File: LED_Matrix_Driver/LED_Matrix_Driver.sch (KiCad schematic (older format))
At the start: 64 parts, among them J1 5V_DC, J2 I2C Bus, J3 LED Anode Rows, J4 Columns 24-31 LED Cathodes, J5 Columns 16-23 LED Cathodes, J6 Columns 8-15 LED Cathodes, J7 Columns 0-7 LED Cathodes, U1 ATmega8-16PU, U2 74HC238, U3 MIC2981, U4 HEF4794B, U5 HEF4794B, U6 HEF4794B, U7 HEF4794B, Y1 16MHz

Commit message: First test commit of ESP32 branch
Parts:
- removed U1: ATmega8-16PU, Package_DIP:DIP-28_W7.62mm_Socket, symbol MCU_Microchip_ATmega:ATmega8-16PU
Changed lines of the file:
@@
 	0    1    1    0
-$EndComp
-$Comp
-L MCU_Microchip_ATmega:ATmega8-16PU U1
-U 1 1 650E955F
-P 3050 5000
-F 0 "U1" H 3050 5000 50  0000 C CNN
-F 1 "ATmega8-16PU" H 3000 4850 50  0000 C CNN
-F 2 "Package_DIP:DIP-28_W7.62mm_Socket" H 3050 5000 50  0001 C CIN
-F 3 "http://ww1.microchip.com/downloads/en/DeviceDoc/atmel-2486-8-bit-avr-microcontroller-atmega8_l_datasheet.pdf" H 3050 5000 50  0001 C CNN
-	1    3050 5000
-	1    0    0    -1
 $EndComp
 Wire Wire Line

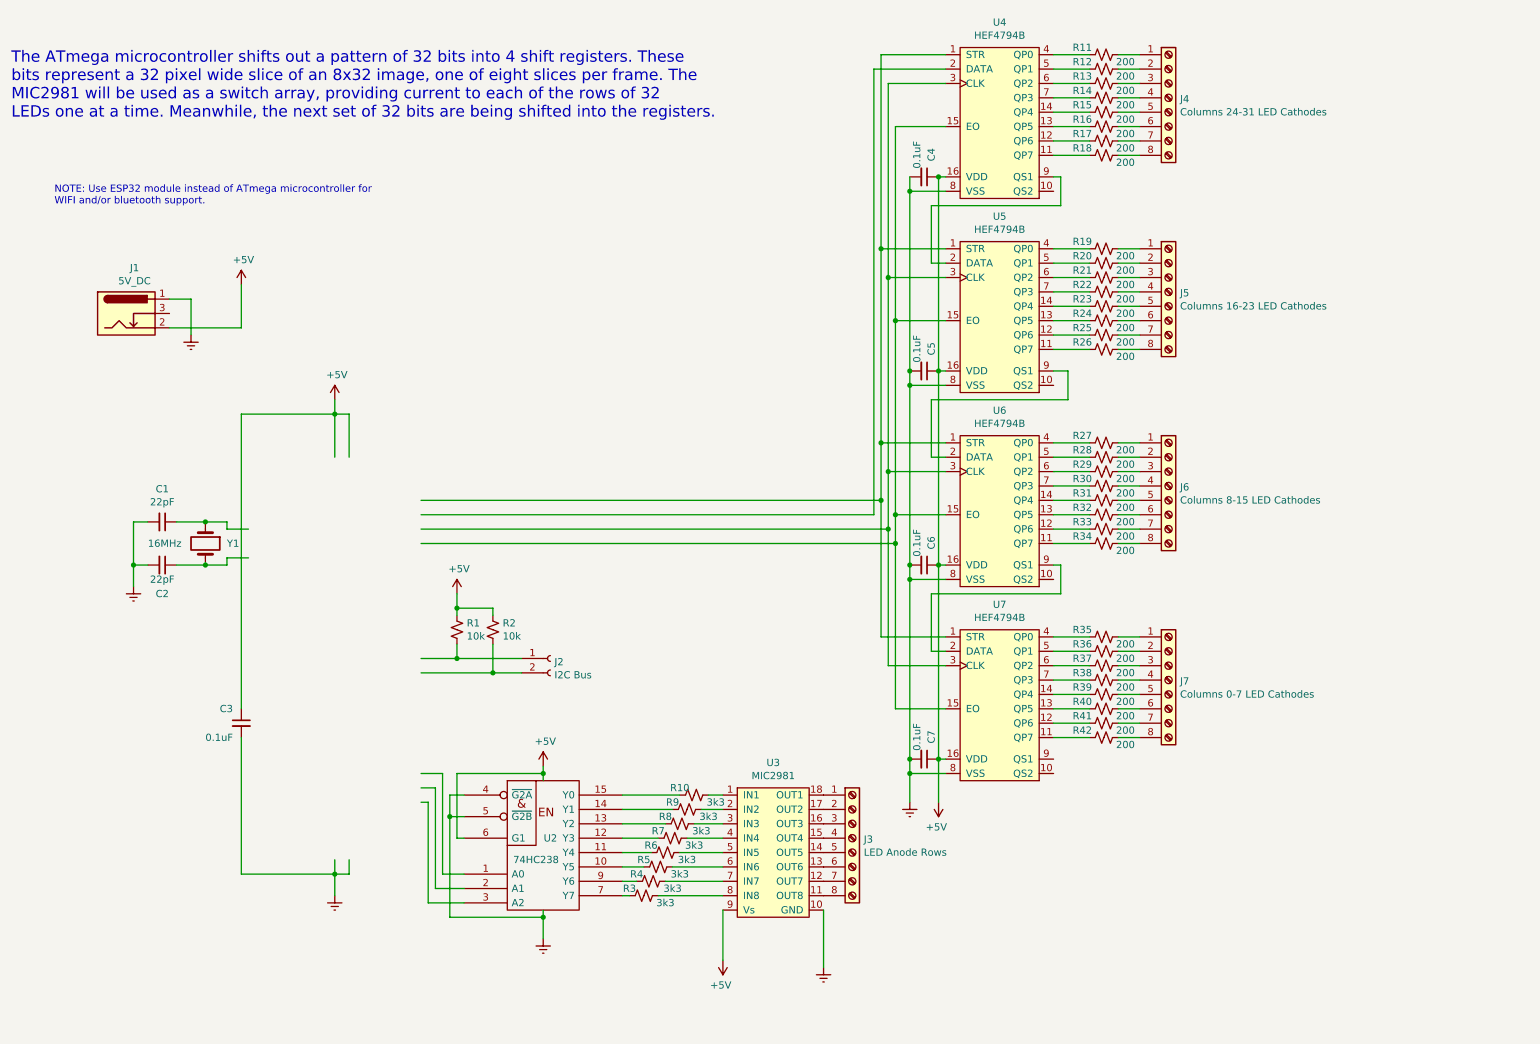
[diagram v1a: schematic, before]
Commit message: Created symbol for ESP32 Devkit and added it to the schematic
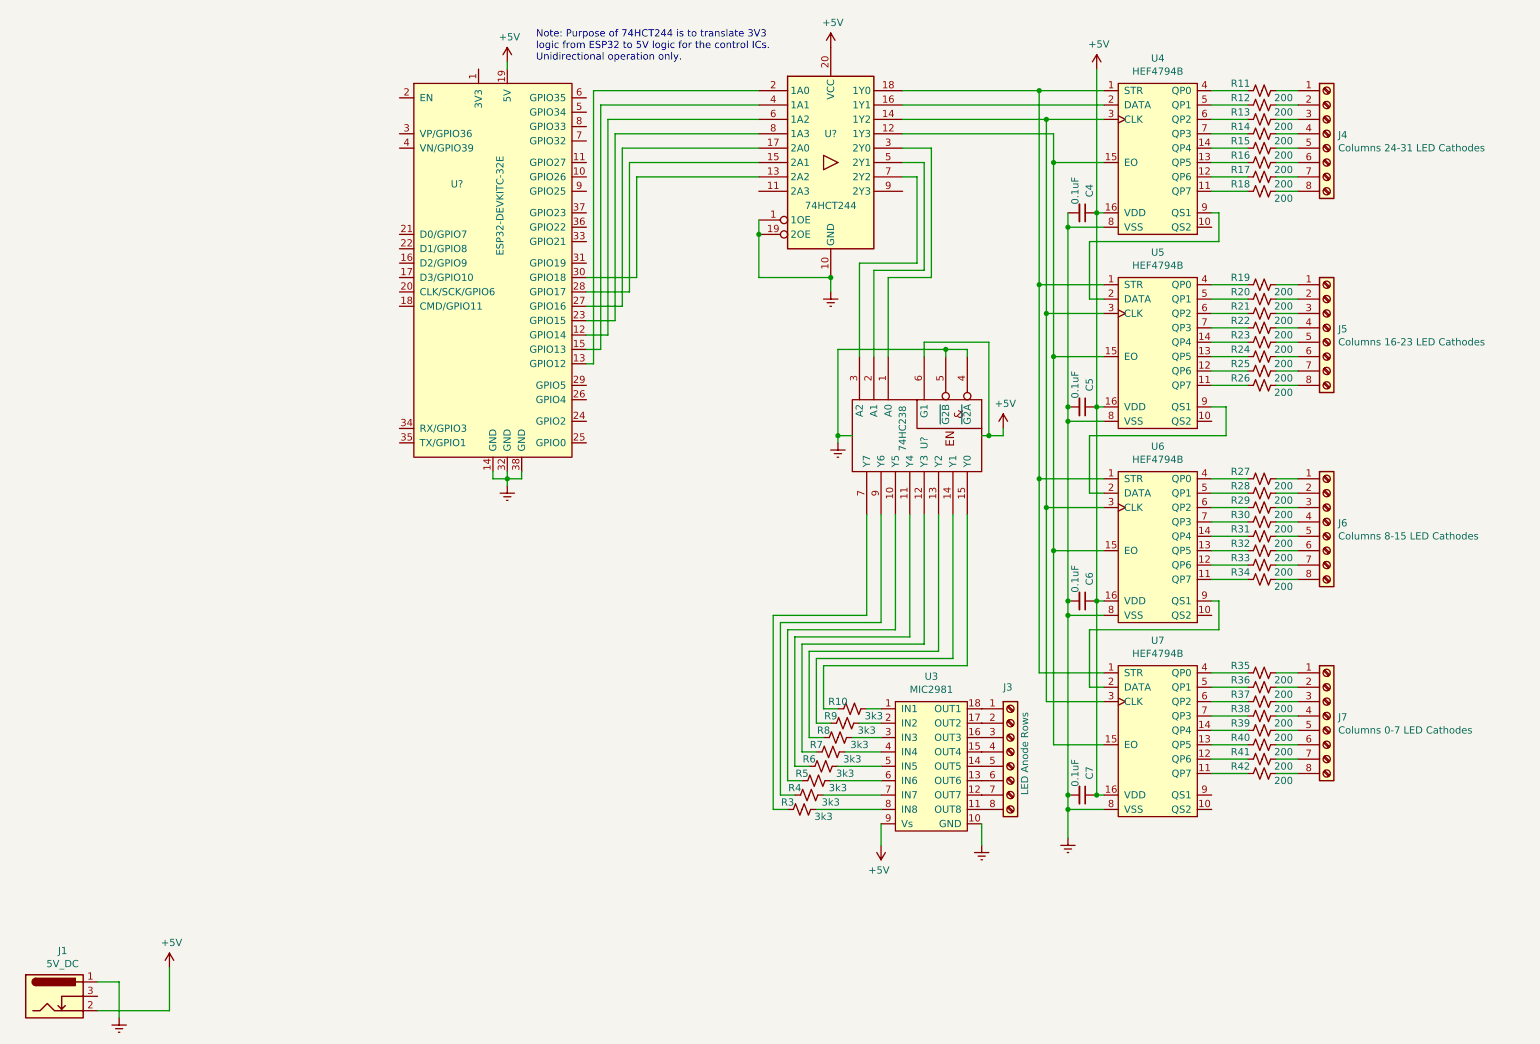
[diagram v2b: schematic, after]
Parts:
- removed C1, C2: 22pF, Capacitor_THT:C_Axial_L3.8mm_D2.6mm_P7.50mm_Horizontal, symbol Device:C_Small
- removed C3: 0.1uF, Capacitor_THT:C_Axial_L3.8mm_D2.6mm_P7.50mm_Horizontal, symbol Device:C_Small
- removed J2: I2C Bus, TerminalBlock_Phoenix:TerminalBlock_Phoenix_MKDS-1,5-2-5.08_1x02_P5.08mm_Horizontal, symbol Connector:Conn_01x02_Female
- removed R1, R2: 10k, Resistor_THT:R_Axial_DIN0204_L3.6mm_D1.6mm_P7.62mm_Horizontal, symbol Device:R_Small_US
- removed U2: 74HC238, Package_DIP:DIP-16_W7.62mm_Socket, symbol 74xx_IEEE:74HC238
- removed Y1: 16MHz, Crystal:Crystal_HC49-U_Vertical, symbol Device:Crystal
- added U?: 74HCT244, symbol 74xx:74HCT244
- added U?: ESP32-DEVKITC-32E, symbol Custom_Symbols:ESP32-DEVKITC-32E
- added U?: 74HC238, Package_DIP:DIP-16_W7.62mm_Socket, symbol 74xx_IEEE:74HC238
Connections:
- wire segments 206 -> 228
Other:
- note added: "Note: Purpose of 74HCT244 is to translate 3V3 \nlogic from ESP32 to 5V logic for the control ICs. \nUnidirectional operation only."
- note removed: "NOTE: Use ESP32 module instead of ATmega microcontroller for\nWIFI and/or bluetooth support."
- note removed: "The ATmega microcontroller shifts out a pattern of 32 bits into 4 shift registers. These\nbits represent a 32 pixel wide slice of an 8x32 image, one of eight slices per frame. The\nMIC2981 will be used as a switch array, providing current to each of the rows of 32\nLEDs one at a time. Meanwhile, the next set of 32 bits are being shifted into the registers."
- moved on the sheet: C4, C5, C6, C7, J1, J3, J4, J5, J6, J7, R10, R11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

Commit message: Big Commit:
- Hardware files are complete
    - Final hardware iteration until further notice.
- Generated new firmware project with Platform.io in VSCode
    - Will use git more with this
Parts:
- removed J1: 5V_DC, Connector_BarrelJack:BarrelJack_Horizontal, symbol Connector:Barrel_Jack_Switch
- added J1: Screw_Terminal_01x02, TerminalBlock_4Ucon:TerminalBlock_4Ucon_1x02_P3.50mm_Horizontal, symbol Connector:Screw_Terminal_01x02
- added R1, R2, R3, R4, R5, R6, R7: 1M, Resistor_THT:R_Axial_DIN0204_L3.6mm_D1.6mm_P7.62mm_Horizontal, symbol Device:R_Small_US
- U1: renamed from U?; footprint (none) -> Arduino:ESP32-DevkitC
- U2: renamed from U?; footprint (none) -> Package_DIP:DIP-20_W7.62mm_Socket
- gave numbers to parts that had none: 1
- renumbered C4 to C1, C5 to C2, C6 to C3, C7 to C4, J3 to J2, J4 to J3, J5 to J4, J6 to J5, J7 to J6, R5 to R10, R6 to R11, R7 to R12, R8 to R13, R9 to R14, R10 to R15, R11 to R16, R12 to R17, R13 to R18, R14 to R19, R15 to R20, R16 to R21, R17 to R22, R18 to R23, R19 to R24, R20 to R25, R21 to R26, R22 to R27, R23 to R28, R24 to R29, R25 to R30, R26 to R31, R27 to R32, R28 to R33, R29 to R34, R30 to R35, R31 to R36, R32 to R37, R33 to R38, R34 to R39, R35 to R40, R36 to R41, R37 to R42, R38 to R43, R39 to R44, R40 to R45, R41 to R46, R42 to R47, R3 to R8, R4 to R9, U4 to U5, U5 to U6, U6 to U7, U7 to U8
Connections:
- net +5V: now also J1.1 (Pin_1)
- net Earth: now also J1.2 (Pin_2), R1.2, R2.2, R3.2, R4.2, R5.2, R6.2, R7.2
- net at U1.30 (GPIO18), U2.13 (2A2): now also R1.1
- net at U1.28 (GPIO17), U2.15 (2A1): now also R2.1
- net at U1.27 (GPIO16), U2.17 (2A0): now also R3.1
- net at U1.13 (GPIO12), U2.2 (1A0): now also R7.1
- net at U1.15 (GPIO13), U2.4 (1A1): now also R6.1
- net at U1.12 (GPIO14), U2.6 (1A2): now also R5.1
- net at U1.23 (GPIO15), U2.8 (1A3): now also R4.1
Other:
- moved on the sheet: U1
